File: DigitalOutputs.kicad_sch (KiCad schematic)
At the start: 4 parts, among them J20 Conn_01x04_Socket, J21 Conn_01x04_Socket, J22 Conn_01x02_Socket

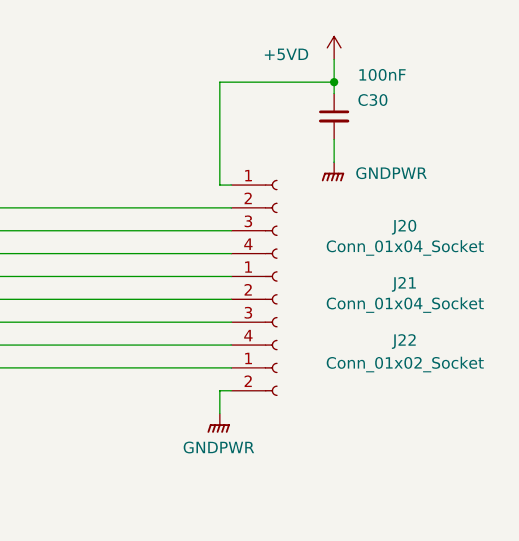
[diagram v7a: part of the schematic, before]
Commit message: Added high speed encoder input circuitry. General tidy and updates to readme
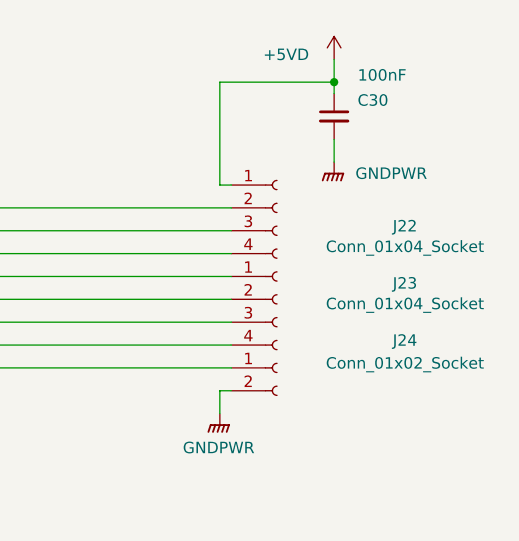
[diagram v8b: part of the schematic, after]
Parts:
- renumbered J20 to J22, J21 to J23, J22 to J24
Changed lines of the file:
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@@
 		(on_board yes)
 		(dnp no)
-		(property "Reference" "#PWR0201"
+		(property "Reference" "#PWR0206"
 			(at 212.09 86.36 0)
 			(effects
@@
 			(project "Remora Nucleo F446ZE Hat"
 				(path "/5473abc6-7b93-43cc-a401-f691c4d7d7cf/a10f9653-3098-46b3-8571-958500eea49a"
-					(reference "#PWR0201")
+					(reference "#PWR0206")
 					(unit 1)
 				)
@@
 		(on_board yes)
 		(dnp no)
-		(property "Reference" "J21"
+		(property "Reference" "J23"
 			(at 219.964 94.742 0)
 			(effects
@@
 			(project "Remora Nucleo F446ZE Hat"
 				(path "/5473abc6-7b93-43cc-a401-f691c4d7d7cf/a10f9653-3098-46b3-8571-958500eea49a"
-					(reference "J21")
+					(reference "J23")
 					(unit 1)
 				)
@@
 		(on_board yes)
 		(dnp no)
-		(property "Reference" "J20"
+		(property "Reference" "J22"
 			(at 219.964 88.392 0)
 			(effects
@@
 			(project "Remora Nucleo F446ZE Hat"
 				(path "/5473abc6-7b93-43cc-a401-f691c4d7d7cf/a10f9653-3098-46b3-8571-958500eea49a"
-					(reference "J20")
+					(reference "J22")
 					(unit 1)
 				)
@@
 		(dnp no)
 		(fields_autoplaced yes)
-		(property "Reference" "#PWR0199"
+		(property "Reference" "#PWR0204"
 			(at 199.39 114.3 0)
 			(effects
@@
 			(project ""
 				(path "/5473abc6-7b93-43cc-a401-f691c4d7d7cf/a10f9653-3098-46b3-8571-958500eea49a"
-					(reference "#PWR0199")
+					(reference "#PWR0204")
 					(unit 1)
 				)
@@
 		(on_board yes)
 		(dnp no)
-		(property "Reference" "#PWR0200"
+		(property "Reference" "#PWR0205"
 			(at 212.09 73.66 0)
 			(effects
@@
 			(project "Remora Nucleo F446ZE Hat"
 				(path "/5473abc6-7b93-43cc-a401-f691c4d7d7cf/a10f9653-3098-46b3-8571-958500eea49a"
-					(reference "#PWR0200")
+					(reference "#PWR0205")
 					(unit 1)
 				)
@@
 		(on_board yes)
 		(dnp no)
-		(property "Reference" "J22"
+		(property "Reference" "J24"
 			(at 219.964 101.092 0)
 			(effects
@@
 			(project "Remora Nucleo F446ZE Hat"
 				(path "/5473abc6-7b93-43cc-a401-f691c4d7d7cf/a10f9653-3098-46b3-8571-958500eea49a"
-					(reference "J22")
-					(unit 1)
-				)
+					(reference "J24")
+					(unit 1)
+				)
